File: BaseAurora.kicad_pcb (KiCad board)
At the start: 2 copper layers, 80 x 100 mm, 43 parts, among them J1 Conn_01x04_Male, J10 Conn_01x03_Male, J11 Screw_Terminal_01x02, J2 Conn_01x05_Male, J3 Screw_Terminal_01x02, J4 Conn_01x04_Male, J5 Conn_01x04_Male, J6 Screw_Terminal_01x02, J7 Screw_Terminal_01x02, J8 Header_1x2, J9 Header_1x2, K1 HK4100F-DC3V-SHG, Q1 2N3906, Q2 PN2222A, U1 ME6217C33M5G, U2 E32-915T20D, U3 4N32M, U4 NodeMCU1.0(ESP-12E)

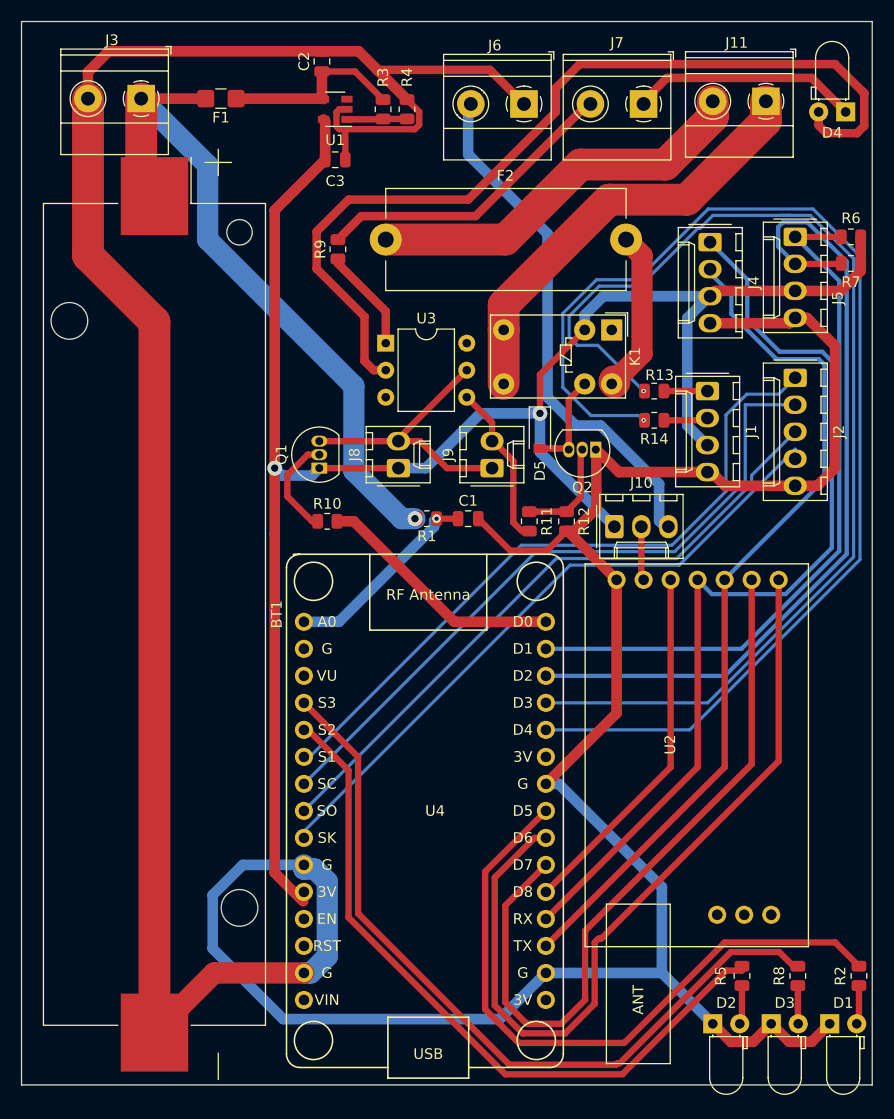
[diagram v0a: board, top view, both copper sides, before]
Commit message: Refatoração do component placement e design das tracks seguindo o novo fator de forma. Exclusão de um dos leds e reposicionamento da conexão NiCr.
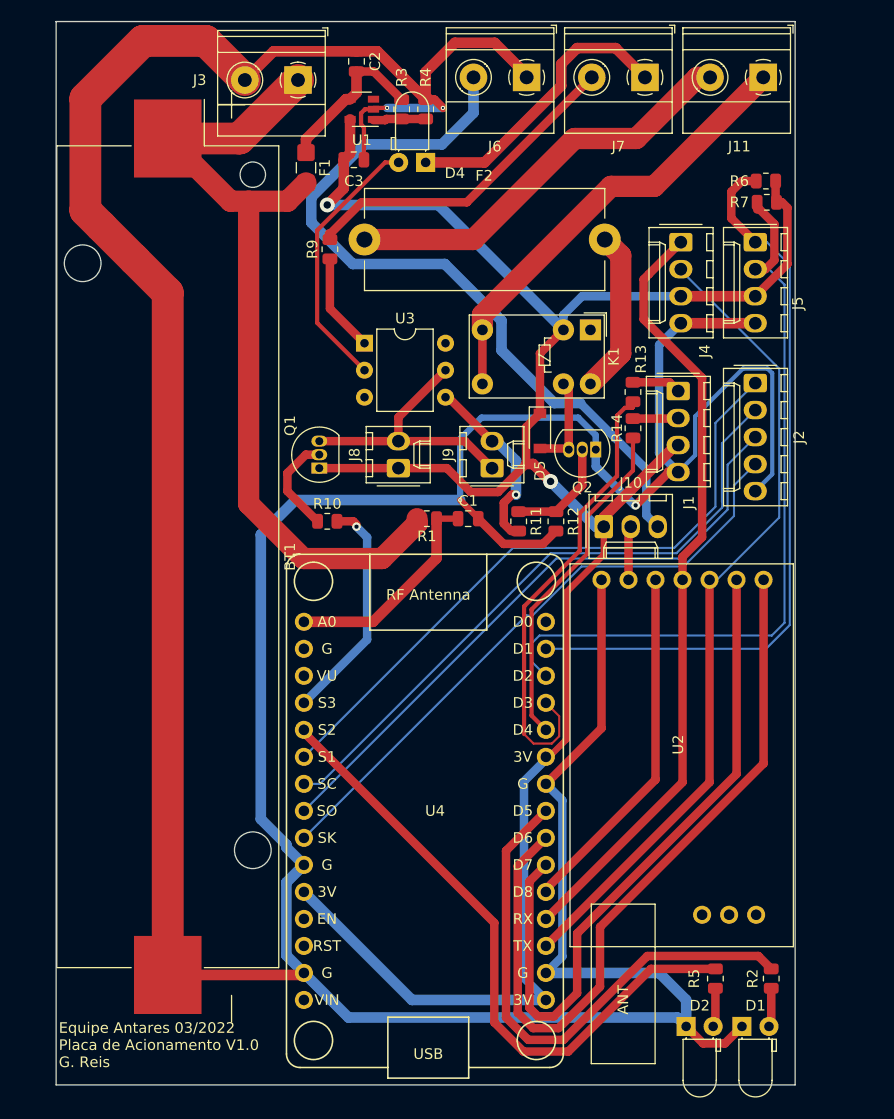
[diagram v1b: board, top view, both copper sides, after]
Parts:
- removed D3: Yellow, LED_THT:LED_D3.0mm_Horizontal_O1.27mm_Z2.0mm
- removed R8: 125, Resistor_SMD:R_0805_2012Metric
- moved D4 39.8 mm to (226.2, 35.5)
- moved J3 14.9 mm to (214.2, 27.8)
- moved F1 10.3 mm to (215.0, 36.0), turned to 270 degrees
- moved R7 9.78 mm to (258.3, 39.2)
- moved R6 9.57 mm to (258.2, 37.2)
- moved D1 8.25 mm to (256.0, 116.8)
- moved R2 8.25 mm to (258.8, 112.2)
- moved BT1 5.56 mm to (202.0, 72.6)
- moved J2 3.78 mm to (257.2, 56.2)
- moved J5 3.78 mm to (257.2, 43.0)
- moved C2 3.25 mm to (219.8, 26.0)
- moved J1 2.75 mm to (250.0, 57.0)
- moved J4 2.75 mm to (250.2, 43.0)
- moved D2 2.51 mm to (250.8, 116.8)
- moved J6 2.51 mm to (235.8, 27.5)
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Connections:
- U4 pad 15: 3V3 -> Net-(U4-Pad15)
- U4 pad 30: NiCr -> Net-(U4-Pad30)
- U4 pad 4: LedAlimentacao -> NiCr
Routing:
- net Net-(R14-Pad1): track 114.4 -> 32.0 mm, vias 1 -> 0
- net LedAlimentacao: track 74.2 -> 0.00 mm
- net Net-(R13-Pad2): track 107.1 -> 43.5 mm, vias 1 -> 0
- net Net-(D4-Pad2): track 86.4 -> 25.3 mm
- net GND: track 388.5 -> 427.0 mm, vias 0 -> 4
- net 3V3: track 176.0 -> 201.2 mm
- net Vext: track 49.4 -> 72.8 mm
- net OutputLora: track 88.6 -> 73.5 mm
- net Vbat: track 66.7 -> 78.9 mm, vias 1 -> 0
- net LedAcionamento: track 62.3 -> 50.6 mm
- net LedErro: track 67.2 -> 60.5 mm
- net GND_ISO: track 21.2 -> 27.8 mm
- net M0Lora: track 77.2 -> 72.1 mm
- net SDA_MASTER: track 77.2 -> 72.2 mm
- net M1Lora: track 69.8 -> 64.9 mm
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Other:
- board size 80 x 100 mm -> 69.5 x 100 mm
- board text added: "Equipe Antares 03/2022 Placa de Acionamento V1.0 G. Reis"

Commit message: Adiciona silk com o logo da equipe
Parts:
- added G***: LOGO, LoRA:AntaresLogo, B.Cu at (201.7, 73.0)

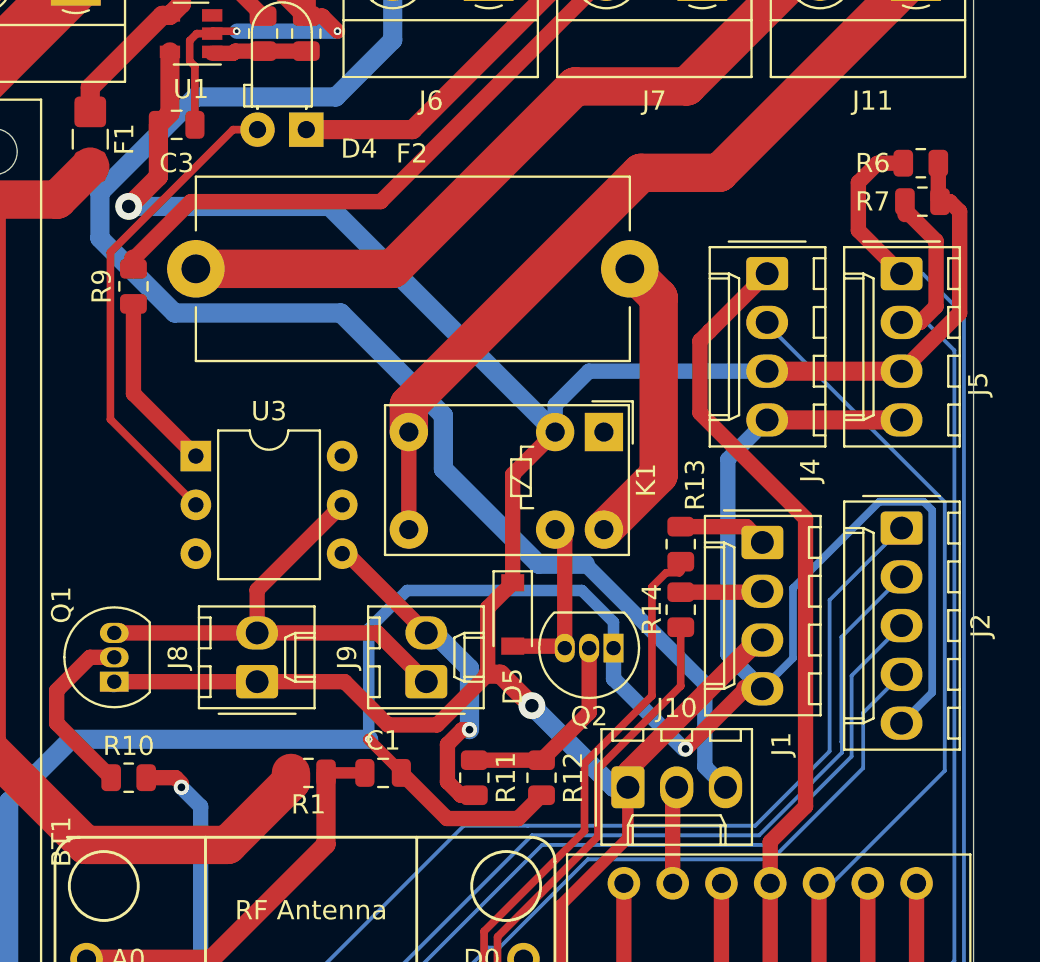
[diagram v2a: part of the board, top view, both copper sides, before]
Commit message: Correção do design de acordo com o DRC
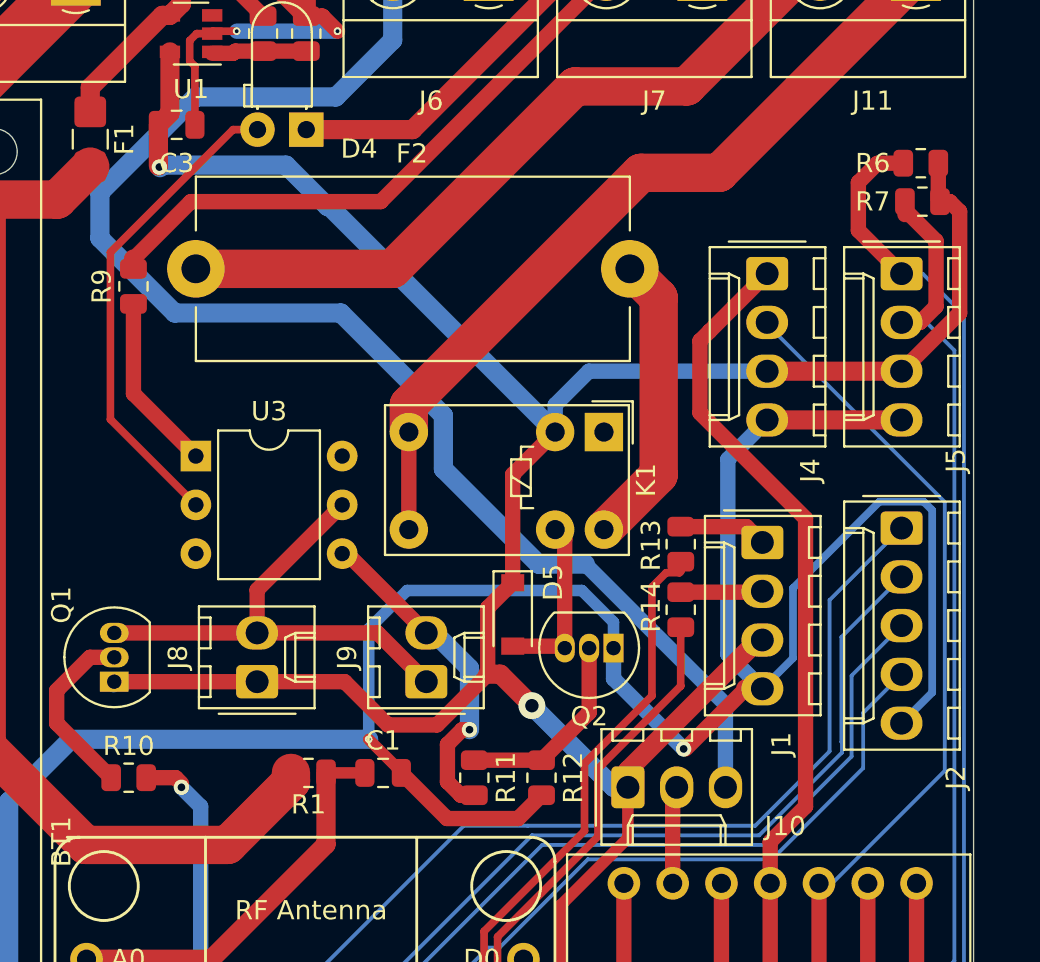
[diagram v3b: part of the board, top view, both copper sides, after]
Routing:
- net 3V3: track 201.2 -> 197.8 mm
